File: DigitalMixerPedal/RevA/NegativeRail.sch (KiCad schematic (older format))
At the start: 3 parts, among them U3 TPS60400

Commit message: hw update
RevA layout completed (draft)
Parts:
- added C41: 1uF, Capacitor_SMD:C_0805_2012Metric_Pad1.15x1.40mm_HandSolder, symbol Device:C
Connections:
- net GNDS: now also C41.2
- net VIN: now also C41.1
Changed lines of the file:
@@
 $Descr A4 11693 8268
 encoding utf-8
-Sheet 17 17
+Sheet 8 17
 Title ""
 Date ""
@@
 AR Path="/5F6F225F/5F6CB881" Ref="U10"  Part="1"
 AR Path="/5F74C2DC/5F6CB881" Ref="U16"  Part="1"
-F 0 "U16" H 5300 3915 50  0000 C CNN
+F 0 "U4" H 5300 3915 50  0000 C CNN
 F 1 "TPS60400" H 5300 3824 50  0000 C CNN
 F 2 "Package_TO_SOT_SMD:SOT-23-5_HandSoldering" H 5300 3823 50  0001 C CNN
@@
 AR Path="/5F6F225F/5F6CBB44" Ref="C15"  Part="1"
 AR Path="/5F74C2DC/5F6CBB44" Ref="C39"  Part="1"
-F 0 "C39" H 4565 3496 50  0000 L CNN
+F 0 "C3" H 4565 3496 50  0000 L CNN
 F 1 "1uF" H 4565 3405 50  0000 L CNN
 F 2 "Capacitor_SMD:C_0805_2012Metric_Pad1.15x1.40mm_HandSolder" H 4488 3300 50  0001 C CNN
@@
 	4450 3650 4900 3650
 Wire Wire Line
-	4900 3150 2950 3150
+	4900 3150 3800 3150
 Text HLabel 2950 3150 0    50   Input ~ 0
 VIN
@@
 AR Path="/5F6F225F/5F6CC20E" Ref="C19"  Part="1"
 AR Path="/5F74C2DC/5F6CC20E" Ref="C40"  Part="1"
-F 0 "C40" H 6540 3471 50  0000 L CNN
+F 0 "C7" H 6540 3471 50  0000 L CNN
 F 1 "1uF" H 6540 3380 50  0000 L CNN
 F 2 "Capacitor_SMD:C_0805_2012Metric_Pad1.15x1.40mm_HandSolder" H 6463 3275 50  0001 C CNN
@@
 	6425 3575 6425 3650
 Connection ~ 6425 3650
+$Comp
+L Device:C C?
+U 1 1 5F6FF6CA
+P 3800 3450
+AR Path="/5F6CB11D/5F6FF6CA" Ref="C?"  Part="1"
+AR Path="/5F6F05C2/5F6FF6CA" Ref="C?"  Part="1"
+AR Path="/5F6F456E/5F6FF6CA" Ref="C?"  Part="1"
+AR Path="/5F6F8B66/5F6FF6CA" Ref="C?"  Part="1"
+AR Path="/5F6E135D/5F6FF6CA" Ref="C41"  Part="1"
+AR Path="/5F6E91E5/5F6FF6CA" Ref="C42"  Part="1"
+AR Path="/5F6EDB29/5F6FF6CA" Ref="C43"  Part="1"
+AR Path="/5F6F225F/5F6FF6CA" Ref="C44"  Part="1"
+AR Path="/5F74C2DC/5F6FF6CA" Ref="C45"  Part="1"
+F 0 "C41" H 3915 3496 50  0000 L CNN
+F 1 "1uF" H 3915 3405 50  0000 L CNN
+F 2 "Capacitor_SMD:C_0805_2012Metric_Pad1.15x1.40mm_HandSolder" H 3838 3300 50  0001 C CNN
+F 3 "~" H 3800 3450 50  0001 C CNN
+	1    3800 3450
+	1    0    0    -1
+$EndComp
+Wire Wire Line
+	3800 3300 3800 3150
+Connection ~ 3800 3150
+Wire Wire Line
+	3800 3150 2950 3150
+Wire Wire Line
+	3800 3600 3800 4400
+$Comp
+L power:GNDS #PWR0107
+U 1 1 5F6FFFBD
+P 3800 4400
+AR Path="/5F6F225F/5F6FFFBD" Ref="#PWR0107"  Part="1"
+AR Path="/5F6E135D/5F6FFFBD" Ref="#PWR0103"  Part="1"
+AR Path="/5F6E91E5/5F6FFFBD" Ref="#PWR0105"  Part="1"
+AR Path="/5F6EDB29/5F6FFFBD" Ref="#PWR0106"  Part="1"
+AR Path="/5F74C2DC/5F6FFFBD" Ref="#PWR0108"  Part="1"
+F 0 "#PWR0108" H 3800 4150 50  0001 C CNN
+F 1 "GNDS" H 3805 4227 50  0000 C CNN
+F 2 "" H 3800 4400 50  0001 C CNN
+F 3 "" H 3800 4400 50  0001 C CNN
+	1    3800 4400
+	1    0    0    -1
+$EndComp
 $EndSCHEMATC

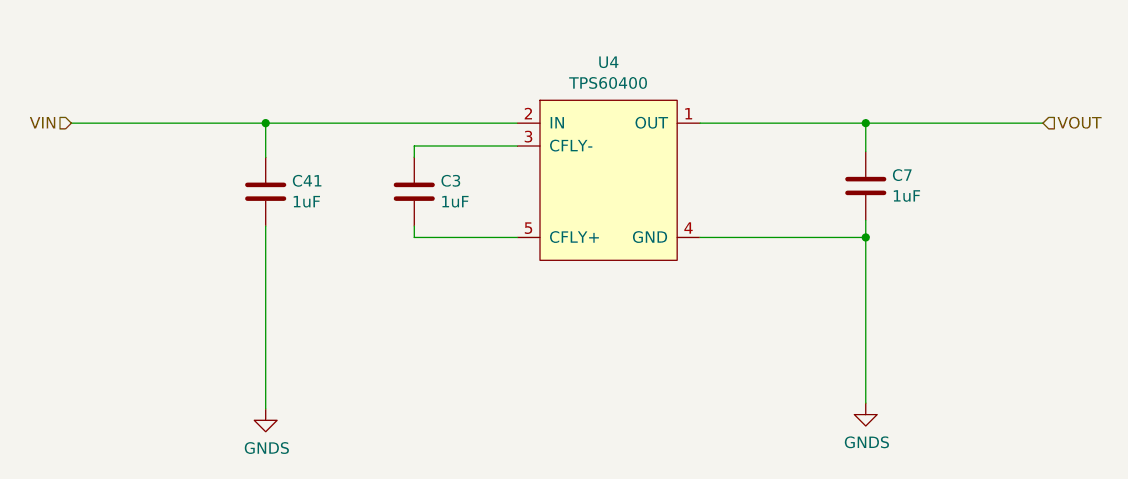
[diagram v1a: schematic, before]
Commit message: updated hw
- added testpoints
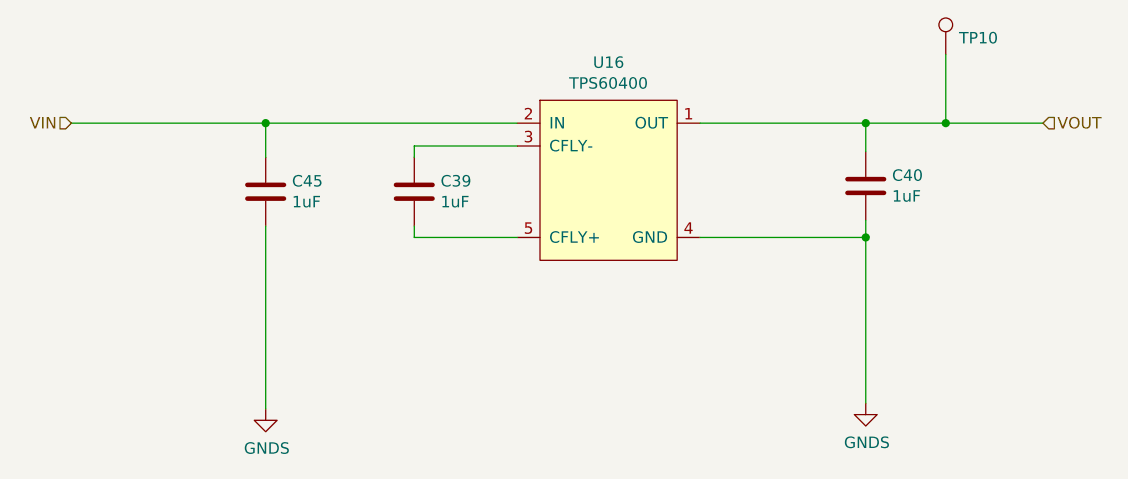
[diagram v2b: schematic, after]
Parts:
- added TP2: TestPoint, TestPoint:TestPoint_Pad_D1.0mm, symbol Connector:TestPoint
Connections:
- net VOUT: now also TP2.1
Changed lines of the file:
@@
 $Descr A4 11693 8268
 encoding utf-8
-Sheet 8 17
+Sheet 17 17
 Title ""
 Date ""
@@
 AR Path="/5F6F225F/5F6CB881" Ref="U10"  Part="1"
 AR Path="/5F74C2DC/5F6CB881" Ref="U16"  Part="1"
-F 0 "U4" H 5300 3915 50  0000 C CNN
+F 0 "U16" H 5300 3915 50  0000 C CNN
 F 1 "TPS60400" H 5300 3824 50  0000 C CNN
 F 2 "Package_TO_SOT_SMD:SOT-23-5_HandSoldering" H 5300 3823 50  0001 C CNN
@@
 AR Path="/5F6F225F/5F6CBB44" Ref="C15"  Part="1"
 AR Path="/5F74C2DC/5F6CBB44" Ref="C39"  Part="1"
-F 0 "C3" H 4565 3496 50  0000 L CNN
+F 0 "C39" H 4565 3496 50  0000 L CNN
 F 1 "1uF" H 4565 3405 50  0000 L CNN
 F 2 "Capacitor_SMD:C_0805_2012Metric_Pad1.15x1.40mm_HandSolder" H 4488 3300 50  0001 C CNN
@@
 AR Path="/5F6F225F/5F6CC20E" Ref="C19"  Part="1"
 AR Path="/5F74C2DC/5F6CC20E" Ref="C40"  Part="1"
-F 0 "C7" H 6540 3471 50  0000 L CNN
+F 0 "C40" H 6540 3471 50  0000 L CNN
 F 1 "1uF" H 6540 3380 50  0000 L CNN
 F 2 "Capacitor_SMD:C_0805_2012Metric_Pad1.15x1.40mm_HandSolder" H 6463 3275 50  0001 C CNN
@@
 Connection ~ 6425 3150
 Wire Wire Line
-	6425 3150 7200 3150
+	6425 3150 6775 3150
 Wire Wire Line
 	6425 3575 6425 3650
@@
 AR Path="/5F6F225F/5F6FF6CA" Ref="C44"  Part="1"
 AR Path="/5F74C2DC/5F6FF6CA" Ref="C45"  Part="1"
-F 0 "C41" H 3915 3496 50  0000 L CNN
+F 0 "C45" H 3915 3496 50  0000 L CNN
 F 1 "1uF" H 3915 3405 50  0000 L CNN
 F 2 "Capacitor_SMD:C_0805_2012Metric_Pad1.15x1.40mm_HandSolder" H 3838 3300 50  0001 C CNN
@@
 	3800 3300 3800 3150
 Connection ~ 3800 3150
-Wire Wire Line
-	3800 3150 2950 3150
 Wire Wire Line
 	3800 3600 3800 4400
@@
 	1    0    0    -1
 $EndComp
+$Comp
+L Connector:TestPoint TP2
+U 1 1 5F727082
+P 6775 2850
+AR Path="/5F6E135D/5F727082" Ref="TP2"  Part="1"
+AR Path="/5F6E91E5/5F727082" Ref="TP4"  Part="1"
+AR Path="/5F6EDB29/5F727082" Ref="TP6"  Part="1"
+AR Path="/5F6F225F/5F727082" Ref="TP8"  Part="1"
+AR Path="/5F74C2DC/5F727082" Ref="TP10"  Part="1"
+F 0 "TP10" H 6833 2922 50  0000 L CNN
+F 1 "TestPoint" H 6833 2877 50  0001 L CNN
+F 2 "TestPoint:TestPoint_Pad_D1.0mm" H 6975 2850 50  0001 C CNN
+F 3 "~" H 6975 2850 50  0001 C CNN
+	1    6775 2850
+	1    0    0    -1
+$EndComp
+Wire Wire Line
+	6775 2850 6775 3150
+Connection ~ 6775 3150
+Wire Wire Line
+	6775 3150 7200 3150
+Wire Wire Line
+	2950 3150 3800 3150
 $EndSCHEMATC
